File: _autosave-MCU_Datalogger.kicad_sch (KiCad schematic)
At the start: 25 parts, among them J1 Conn_01x02_Pin, U1 24LC1025, U2 24LC1025, U3 DS1337S_, U4 ATMEGA328P-AU, Y1 32.768kHz, Y2 16MHz

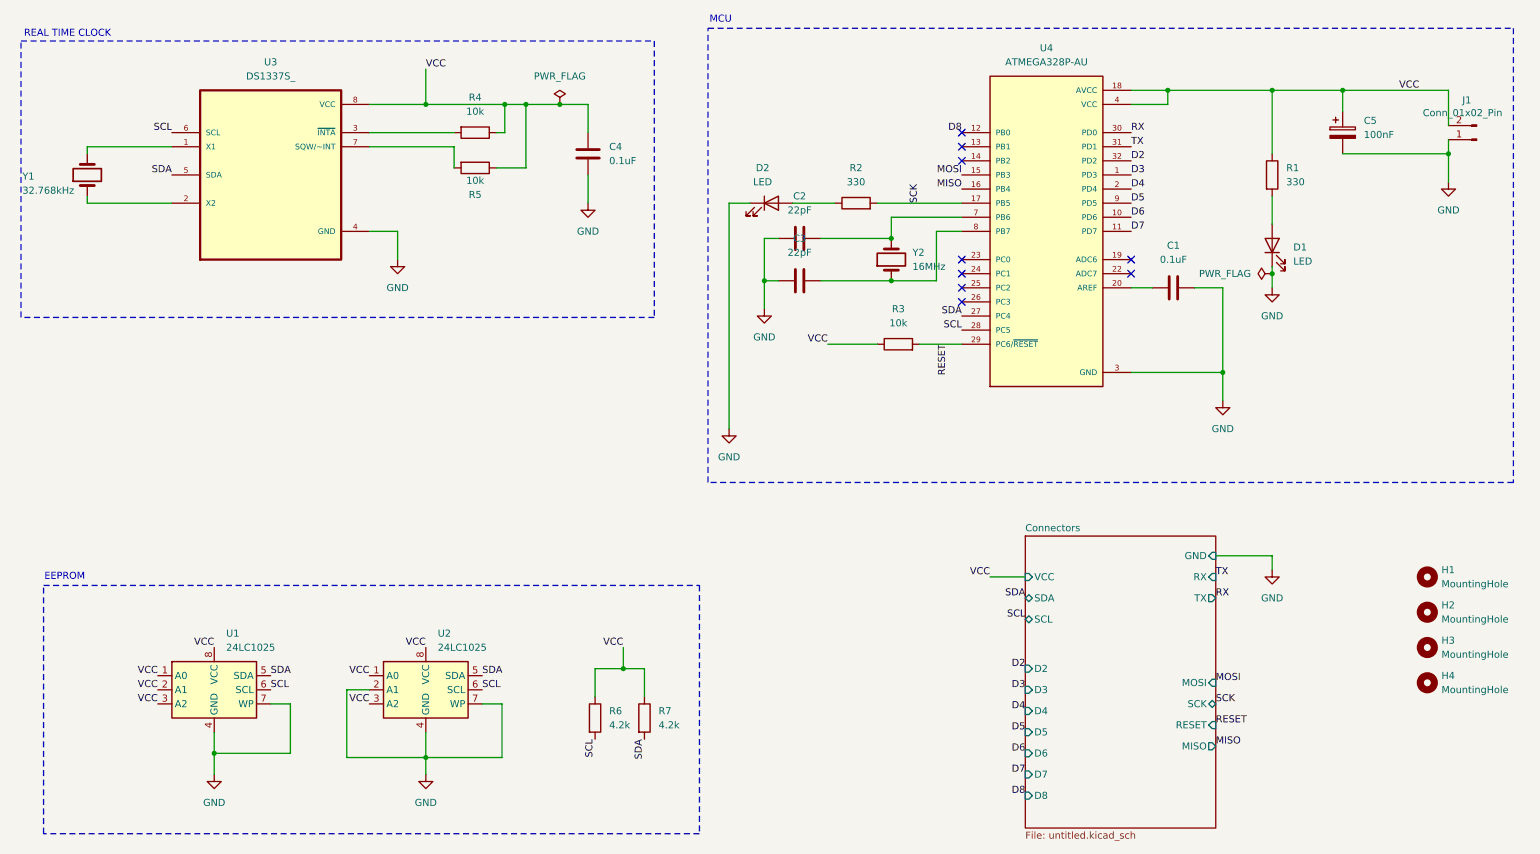
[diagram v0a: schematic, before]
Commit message: Completed PCB Setup and Design
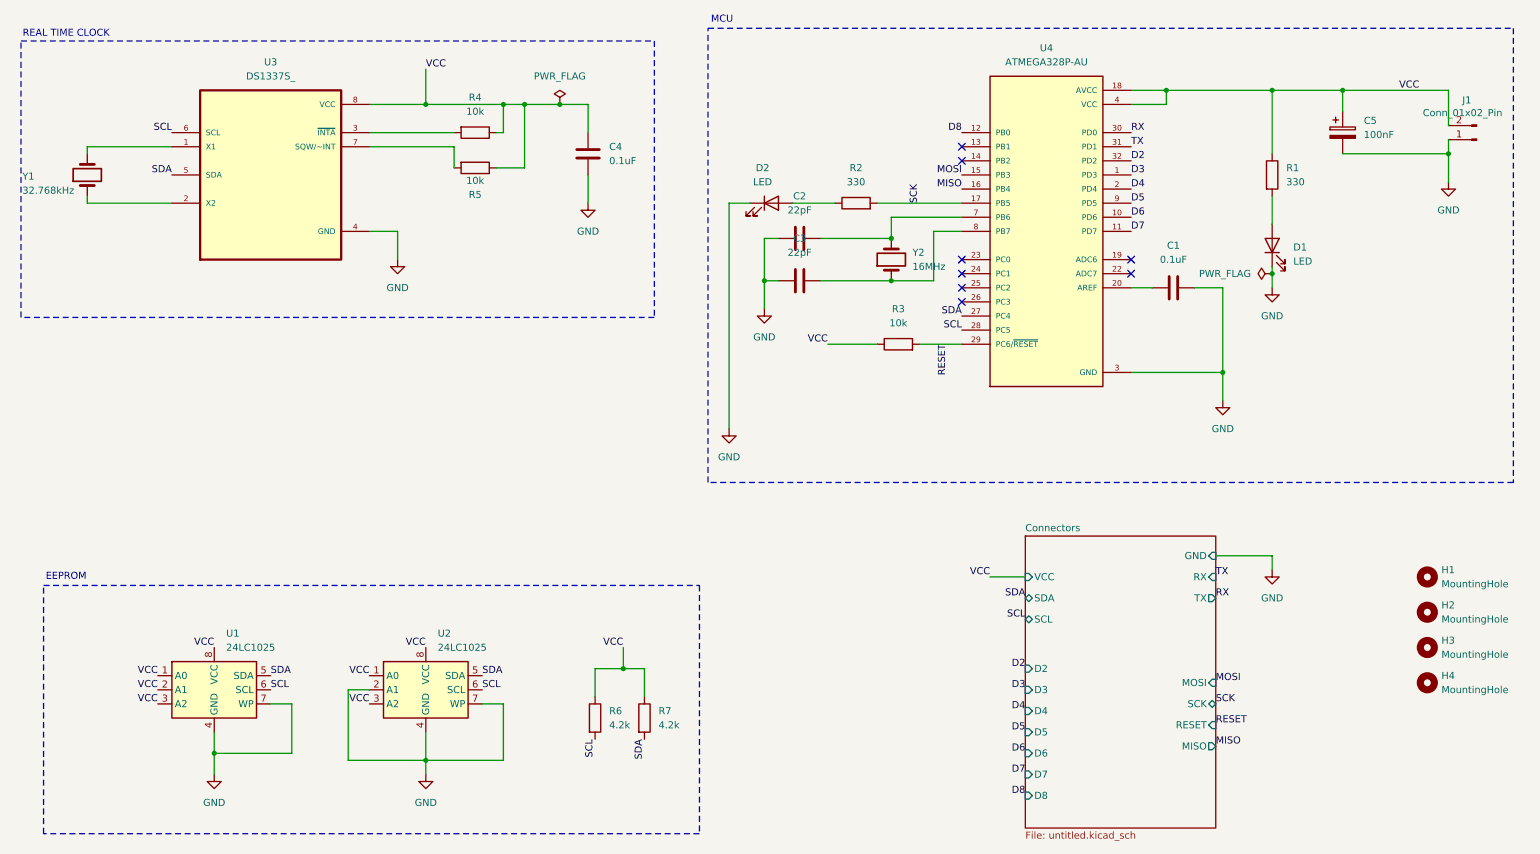
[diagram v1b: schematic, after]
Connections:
- no-connect marks 9 -> 8
